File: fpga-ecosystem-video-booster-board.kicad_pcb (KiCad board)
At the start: 4 copper layers, 41.5 x 41.5 mm, 105 parts, among them J1 0473460001, J10 61300411121, J2 HDMI-PE10-19-LF, J3 HDMI-PE10-19-LF, J4 M20-9990246, J5 M20-9990246, J6 685119134923_, J7 M20-9990246, J8 M20-9990246, J9 685119134923_, Q1 BSS138-7-F, Q2 BSS138-7-F, U1 PTN3363, U2 EFM32HG309, U3 PTN3363, U4 LP2985-33DBVR

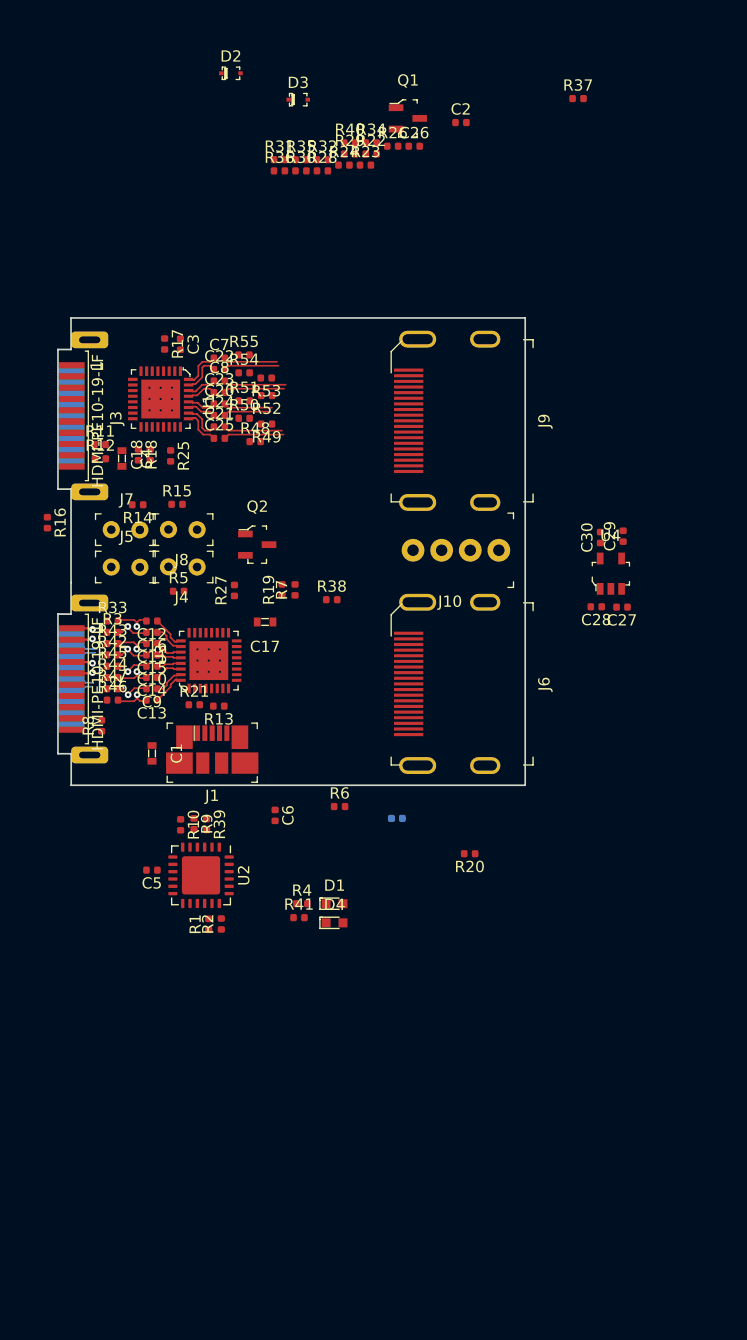
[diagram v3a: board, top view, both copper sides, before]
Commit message: Component layout for double, one sided dongle
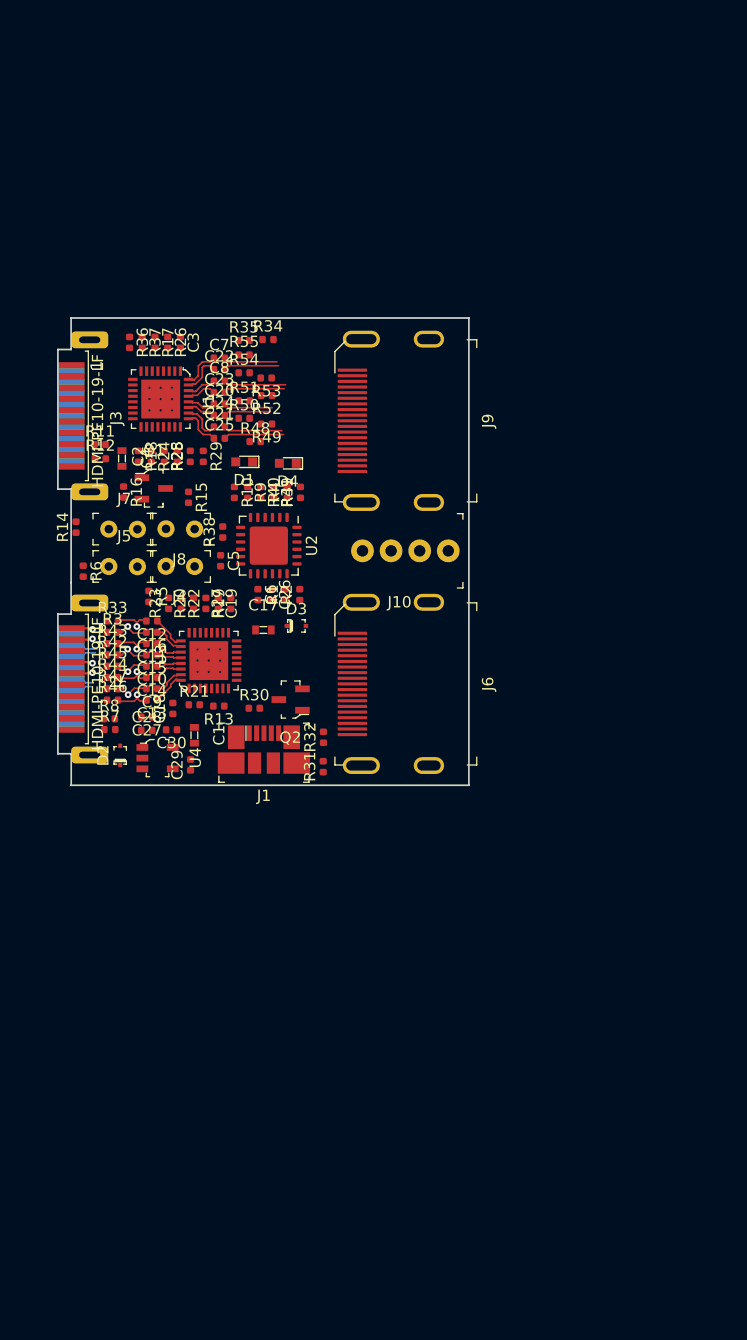
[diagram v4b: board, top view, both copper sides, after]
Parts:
- C19: moved to F.Cu
- moved D2 61.4 mm to (119.0, 97.3), turned to 90 degrees
- moved R31 54.0 mm to (137.1, 98.3), turned to 90 degrees
- moved R32 51.3 mm to (137.1, 95.7), turned to 90 degrees
- moved R30 47.9 mm to (130.9, 93.2)
- moved D3 46.7 mm to (134.7, 85.8)
- moved R37 44.4 mm to (121.0, 60.7), turned to 270 degrees
- moved U4 43.5 mm to (122.3, 97.6), turned to 270 degrees
- moved C29 43.5 mm to (125.3, 98.2)
- moved R22 43.3 mm to (124.4, 83.8), turned to 270 degrees
- moved C27 43.3 mm to (121.4, 94.0)
- moved R23 42.7 mm to (123.3, 83.8), turned to 90 degrees
- moved C26 41.8 mm to (132.5, 83.1), turned to 270 degrees
- moved C30 41.7 mm to (123.6, 95.1), turned to 180 degrees
- moved C28 41.4 mm to (121.4, 95.1), turned to 0 degrees
- moved D4 41.0 mm to (133.9, 71.4), turned to 180 degrees
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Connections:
- R11 pad 2: /TX_SDA -> /RX_SDA
- R12 pad 2: /TX_SCL -> /RX_SCL
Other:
- board size 41.5 x 41.5 mm -> 36.5 x 41.5 mm
